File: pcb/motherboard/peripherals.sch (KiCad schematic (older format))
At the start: 30 parts, among them J17 WIFI-GPIO, J3 DB PWR, J5 Micro_SD, J9 DB I/O, U2 DS3231M, U4 ATWINC1500-MR210PB, U5 74X4050, U6 AP2112K-3.3, U7 74X4050

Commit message: Adjusted page size for motherboard schematic
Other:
- moved on the sheet: B1, C14, C19, C20, C21, C27, J3, J5, J9, R11, R12, R13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

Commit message: Updated PCB design
+ Completed daughterboard PCB layout.
* Corrected soldermask clerance on front panel pcb.
- Removed input resistor on DIN for RGB lamp board.
* Modified PCB layout for PSU board.
* Updated gerber files.
* Updated schematics pdf, BOM.
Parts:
- added J18: DB-C, conn-header:HDR-M-1x02, symbol connectors:HEADER-1x02
- B1: footprint conn-power:BC501SM -> conn-power:S8411-45R; Part BC501SM -> S8411-45R
- J3: value DB PWR -> DB-B
- J5: Part - -> 475710001
- J9: value DB I/O -> DB-A
- U2: value DS3231M -> DS3231MZ
- U5, U7: value 74X4050 -> CD74HC4050PWR; footprint smt-sop:SSOP16 -> smt-sop:TSSOP16; symbol ic-logic:74X4050 -> ic-logic:74?4050
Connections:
- wire segments 172 -> 176
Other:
- note added: "I2C Addr. : 0xD0"
- moved on the sheet: B1, C14, C15, C16, C17, C18, C19, C20, C21, C27, C9, J17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

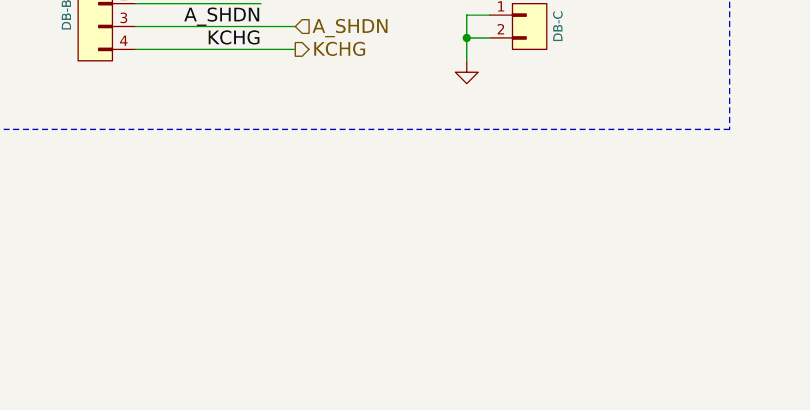
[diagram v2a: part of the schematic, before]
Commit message: Replaced battery holder for Harwin S8411-45R
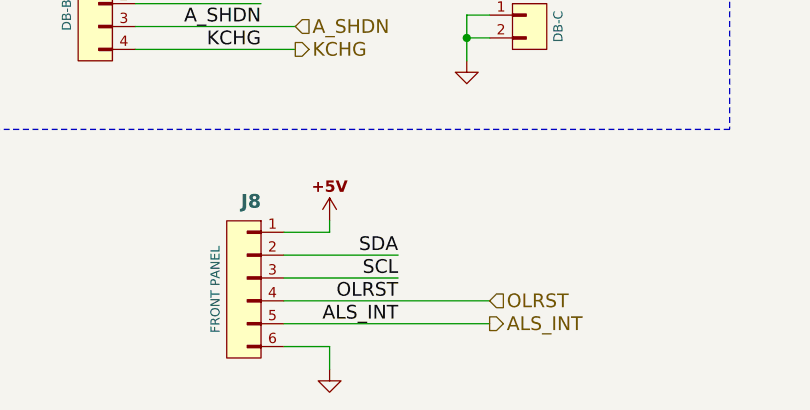
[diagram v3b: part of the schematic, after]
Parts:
- added J8: FRONT PANEL, conn-wire-pads:WP-EDGE-RL-50mil-1x06, symbol connectors:HEADER-1x06
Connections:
- net +5V: now also J8.1 (P1)
- net GND: now also J8.6 (P6)
- net SCL: now also J8.3 (P3)
- net SDA: now also J8.2 (P2)
- new net ALS_INT: J8.5 (P5)
- new net OLRST: J8.4 (P4)
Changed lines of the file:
@@
 Text Notes 1650 7700 0    60   ~ 0
 I2C Addr. : 0xD0
+$Comp
+L connectors:HEADER-1x06 J?
+U 1 1 5BBB9765
+P 5300 7300
+AR Path="/5BBB9765" Ref="J?"  Part="1"
+AR Path="/579732DD/5BBB9765" Ref="J8"  Part="1"
+F 0 "J8" H 5250 7650 60  0000 L BNB
+F 1 "FRONT PANEL" V 5450 7300 40  0000 C CNN
+F 2 "conn-wire-pads:WP-EDGE-RL-50mil-1x06" H 5300 7300 60  0001 C CNN
+F 3 "" H 5300 7300 60  0001 C CNN
+F 4 "-" H 5250 7750 40  0001 L BNN "Part"
+F 5 "Virtual" H 5250 7850 40  0001 L BNN "Family"
+	1    5300 7300
+	-1   0    0    -1
+$EndComp
+$Comp
+L power:+5V #PWR?
+U 1 1 5BBB976C
+P 5650 7000
+AR Path="/5BBB976C" Ref="#PWR?"  Part="1"
+AR Path="/579732DD/5BBB976C" Ref="#PWR0131"  Part="1"
+F 0 "#PWR0131" H 5650 7225 30  0001 C CNN
+F 1 "+5V" V 5575 7000 30  0001 C CNN
+F 2 "" H 5650 7000 60  0000 C CNN
+F 3 "" H 5650 7000 60  0000 C CNN
+	1    5650 7000
+	1    0    0    -1
+$EndComp
+Wire Wire Line
+	5650 7000 5650 7050
+Wire Wire Line
+	5650 7050 5450 7050
+$Comp
+L power:GND #PWR?
+U 1 1 5BBB9774
+P 5650 7650
+AR Path="/5BBB9774" Ref="#PWR?"  Part="1"
+AR Path="/579732DD/5BBB9774" Ref="#PWR0132"  Part="1"
+F 0 "#PWR0132" H 5650 7700 30  0001 C CNN
+F 1 "GND" H 5650 7525 30  0001 C CNN
+F 2 "" H 5650 7650 60  0000 C CNN
+F 3 "" H 5650 7650 60  0000 C CNN
+	1    5650 7650
+	1    0    0    -1
+$EndComp
+Wire Wire Line
+	5450 7550 5650 7550
+Wire Wire Line
+	5650 7550 5650 7650
+Wire Wire Line
+	5450 7150 5950 7150
+Wire Wire Line
+	5450 7250 5950 7250
+Text Label 5950 7150 2    60   ~ 0
+SDA
+Text Label 5950 7250 2    60   ~ 0
+SCL
+Text Label 5950 7350 2    60   ~ 0
+OLRST
+Text Label 5950 7450 2    60   ~ 0
+ALS_INT
+Text HLabel 6350 7350 2    60   Input ~ 0
+OLRST
+Text HLabel 6350 7450 2    60   Output ~ 0
+ALS_INT
+Wire Wire Line
+	5450 7350 6350 7350
+Wire Wire Line
+	5450 7450 6350 7450
 $EndSCHEMATC

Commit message: Fix: Wrong footprint for R20-22 and C14
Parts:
- C14: footprint smt:R-0603 -> smt:C-0603
- R22: footprint smt:C-0603 -> smt:R-0603
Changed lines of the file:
@@
 F 0 "C14" H 708 6742 60  0000 L CNB
 F 1 "100nF" H 708 6647 45  0000 L CNN
-F 2 "smt:R-0603" H 630 6540 40  0001 L CNN
+F 2 "smt:C-0603" H 630 6540 40  0001 L CNN
 F 3 "" H 630 6460 45  0001 L CNN
 F 4 "-" H 640 6865 45  0001 L CNN "Part"
@@
 F 0 "R22" H 8100 4635 60  0000 C CNB
 F 1 "10k" H 8100 4475 40  0000 C CNN
-F 2 "smt:C-0603" H 8100 4410 40  0001 C CNN
+F 2 "smt:R-0603" H 8100 4410 40  0001 C CNN
 F 3 "" H 8100 4650 60  0000 C CNN
 F 4 "-" H 8100 4710 45  0001 C CNN "Part"

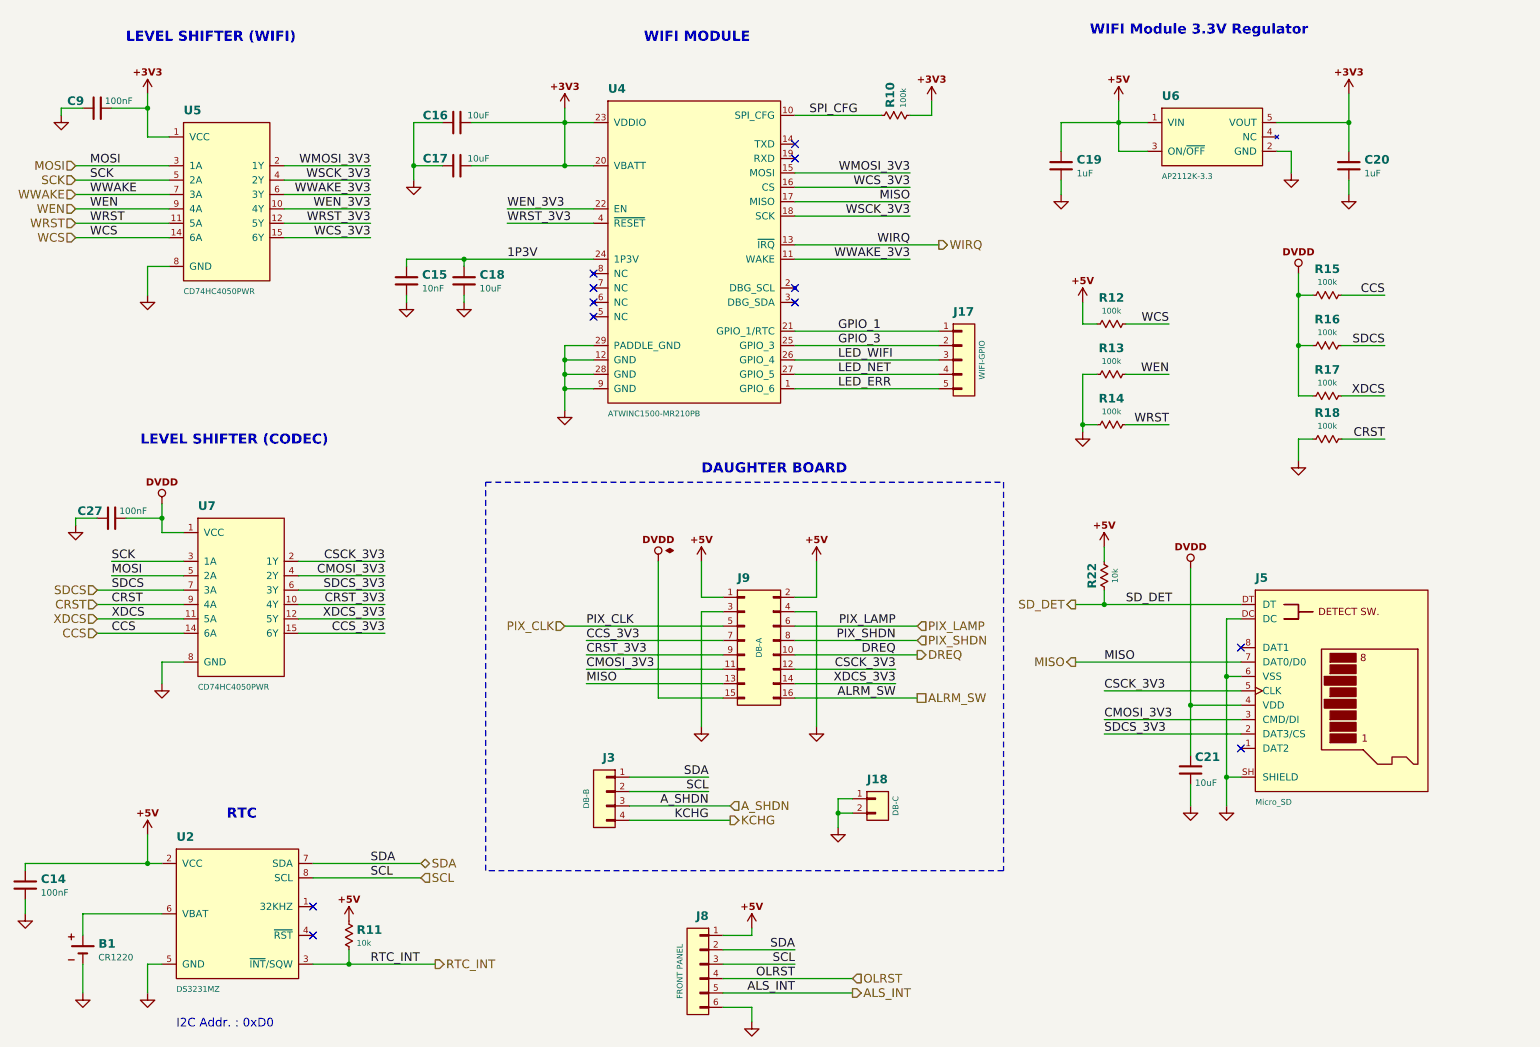
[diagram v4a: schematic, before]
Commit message: Corrected solder mask clearance
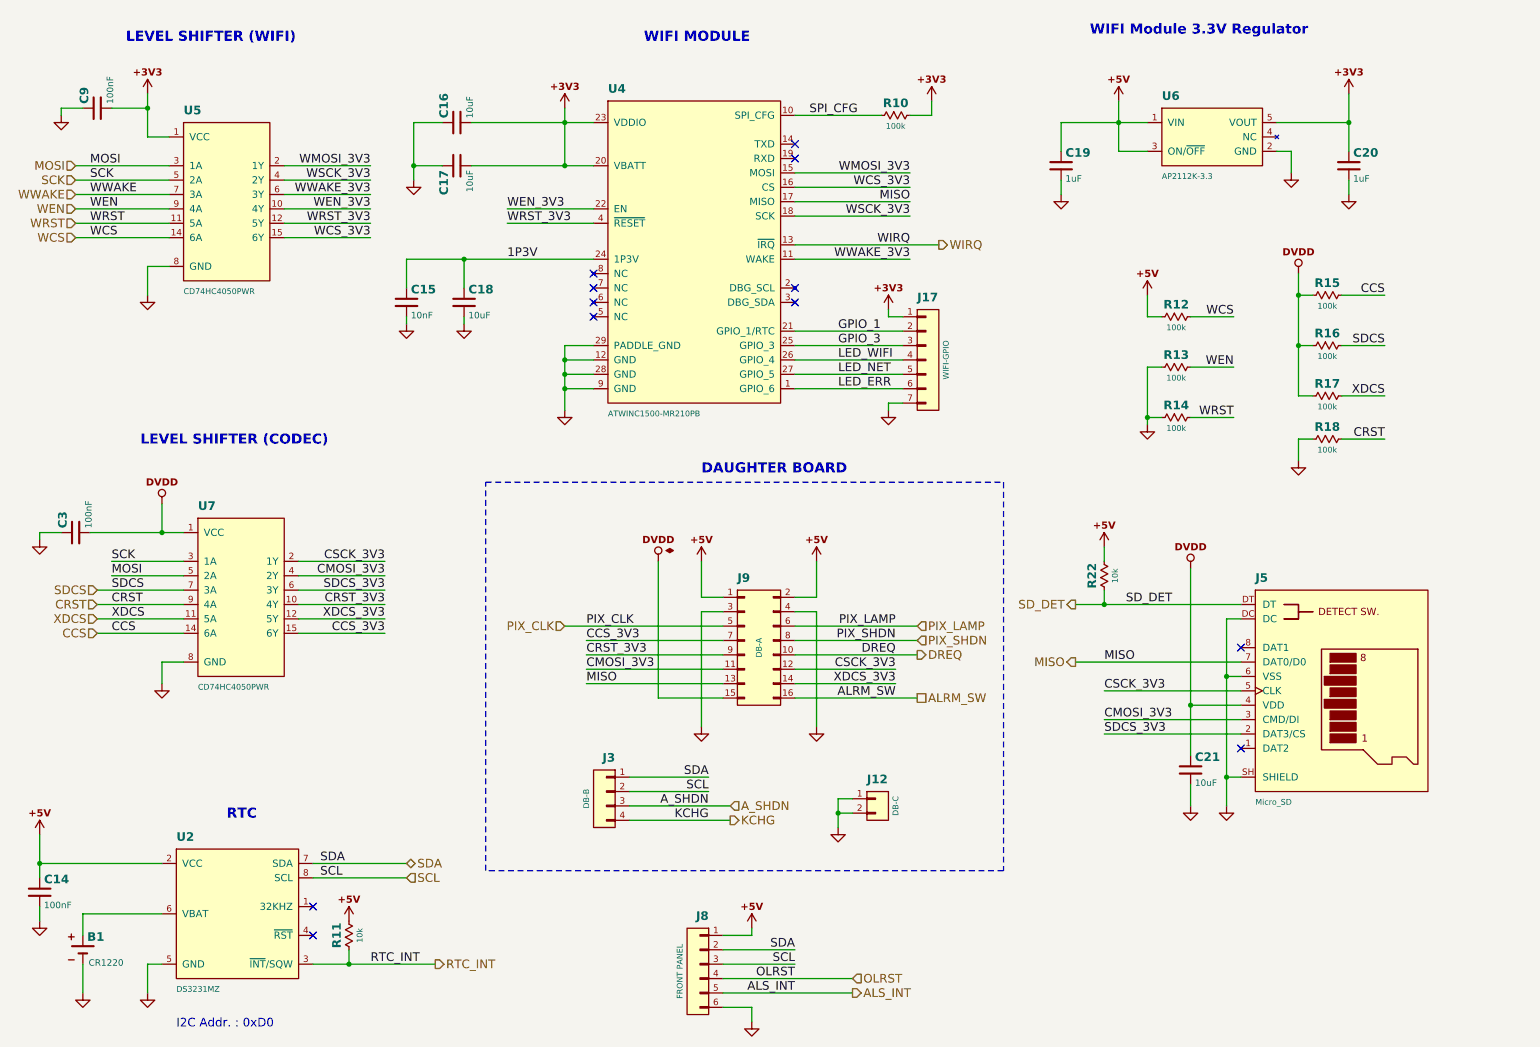
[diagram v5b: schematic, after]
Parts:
- removed J17: WIFI-GPIO, conn-wire-pads:WP-50mil-1x05, symbol connectors:HEADER-1x05
- added J17: WIFI-GPIO, conn-wire-pads:WP-40mil-1x07, symbol connectors:HEADER-1x07
- renumbered C27 to C3, J18 to J12
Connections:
- net +3V3: now also C16.1, C17.1, C9.1, J17.1 (P1); no longer C16.2, C17.2, C9.2
- net +5V: now also R11.2; no longer R11.1
- net DVDD: now also C3.1; no longer C3.2
- net GND: now also C16.2, C17.2, C3.2, C9.2, J17.7 (P7); no longer C16.1, C17.1, C3.1, C9.1
- net GPIO_1: now also J17.2 (P2)
- net GPIO_3: now also J17.3 (P3)
- net LED_ERR: now also J17.6 (P6)
- net LED_NET: now also J17.5 (P5)
- net LED_WIFI: now also J17.4 (P4)
- net RTC_INT: now also R11.1; no longer R11.2
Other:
- moved on the sheet: C14, C15, C18, C3, R12, R13, R14
